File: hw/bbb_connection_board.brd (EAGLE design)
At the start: 100 x 80 mm, 2 parts, among them P8 MA23-2

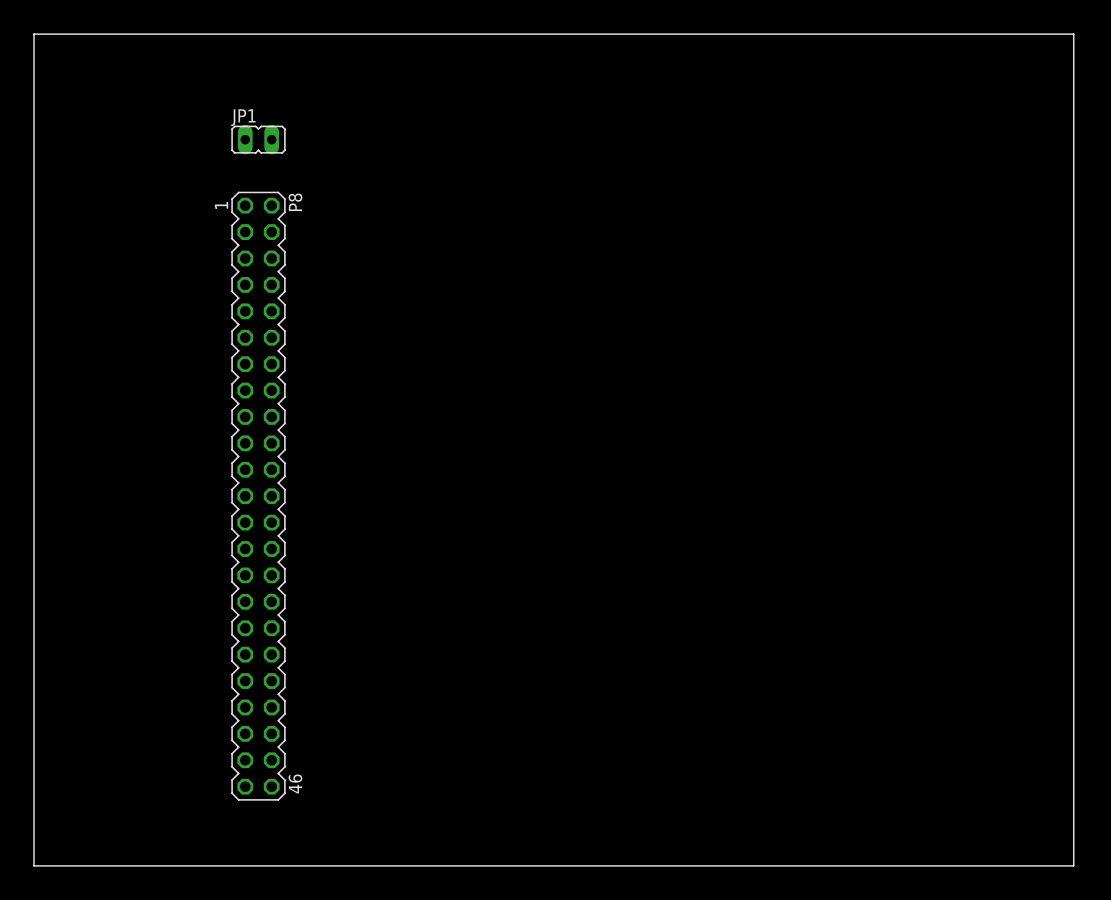
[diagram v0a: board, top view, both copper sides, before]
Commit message: schematic of bbb connection board
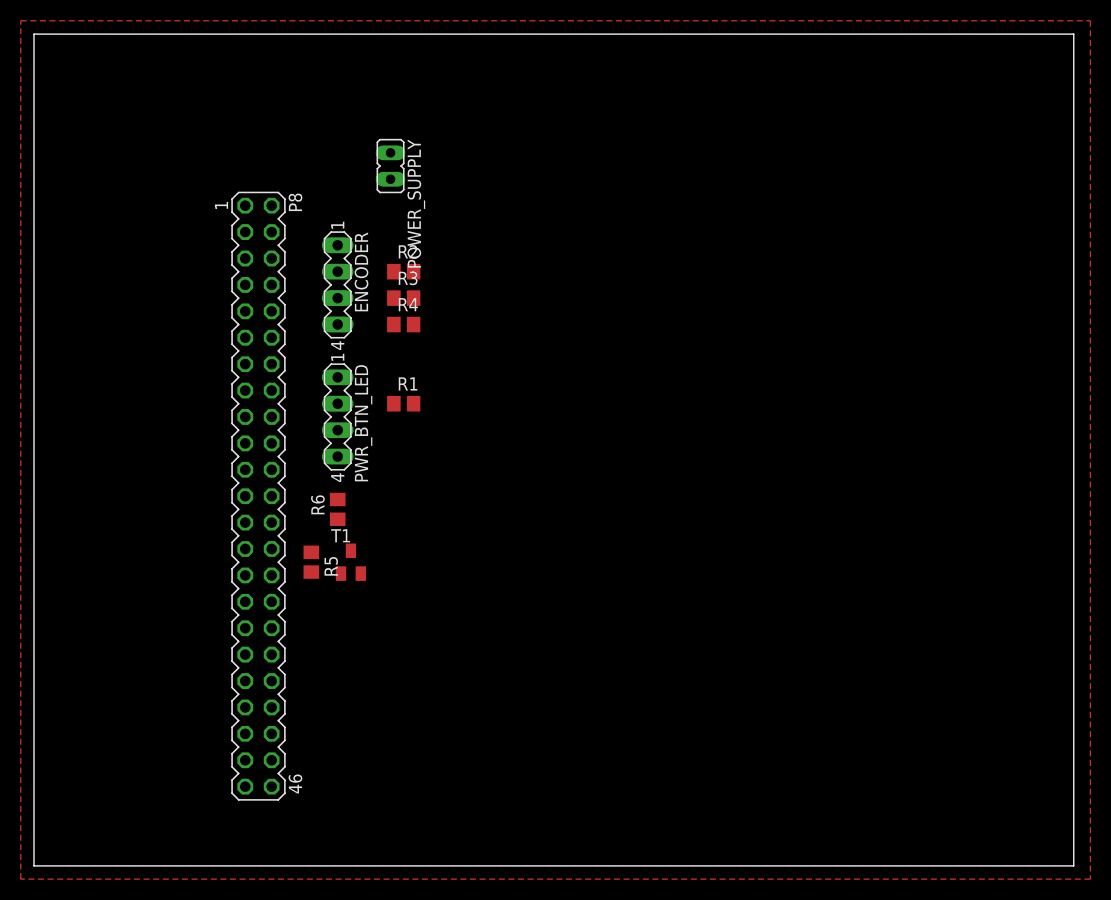
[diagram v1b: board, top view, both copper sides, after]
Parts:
- removed JP1: (no value), jumper:JP1
- added ENCODER, PWR_BTN_LED: (no value), con-lstb:MA04-1
- added POWER_SUPPLY: (no value), jumper:JP1
- added R1, R2, R3, R4, R5: 10k, rcl:R0805
- added R6: 330R, rcl:R0805
- added T1: (no value), transistor:SOT23-BEC
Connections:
- removed net ENCODER_TASTER: P8.8
- removed net PWR_TASTER: P8.7
- new net ENCODER_BTN: ENCODER.2, P8.8, R2.1
- new net LED_OUT: PWR_BTN_LED.4, R6.2
- new net N$1: R5.2, T1.B
- new net N$3: R6.1, T1.C
- new net PWR_BTN: P8.7, PWR_BTN_LED.2, R1.1
- net +3V3: now also POWER_SUPPLY.2, PWR_BTN_LED.3, R1.2, R2.2, R3.2, R4.2; no longer JP1.2
- net ENCODER_A: now also ENCODER.3, R3.1
- net ENCODER_B: now also ENCODER.4, R4.1
- net GND: now also ENCODER.1, POWER_SUPPLY.1, PWR_BTN_LED.1, T1.E; no longer JP1.1
- net PWR_LED: now also R5.1
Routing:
- added copper zone on layer 1, net GND
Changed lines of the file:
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@@
 <setting verticaltext="up"/>
 </settings>
-<grid distance="0.05" unitdist="inch" unit="inch" style="lines" multiple="1" display="yes" altdistance="0.025" altunitdist="inch" altunit="inch"/>
+<grid distance="0.05" unitdist="inch" unit="mil" style="lines" multiple="1" display="yes" altdistance="0.025" altunitdist="inch" altunit="inch"/>
 <layers>
 <layer number="1" name="Top" color="4" fill="1" visible="yes" active="yes"/>
@@
 <elements>
 <element name="P8" library="con-lstb-mod" package="MA23-2" value="MA23-2" x="20.32" y="63.5" rot="R270"/>
-<element name="JP1" library="jumper" package="JP1" value="" x="21.59" y="69.85" rot="R270"/>
+<element name="POWER_SUPPLY" library="jumper" package="JP1" value="" x="34.29" y="67.31" rot="R180"/>
+<element name="R1" library="rcl" package="R0805" value="10k" x="35.56" y="44.45"/>
+<element name="R2" library="rcl" package="R0805" value="10k" x="35.56" y="57.15"/>
+<element name="R3" library="rcl" package="R0805" value="10k" x="35.56" y="54.61"/>
+<element name="R4" library="rcl" package="R0805" value="10k" x="35.56" y="52.07"/>
+<element name="ENCODER" library="con-lstb" package="MA04-1" value="" x="29.21" y="55.88" rot="R270">
+<attribute name="OC_NEWARK" value="unknown" x="29.21" y="55.88" size="1.778" layer="27" rot="R270" display="off"/>
+<attribute name="MPN" value="" x="29.21" y="55.88" size="1.778" layer="27" rot="R270" display="off"/>
+<attribute name="MF" value="" x="29.21" y="55.88" size="1.778" layer="27" rot="R270" display="off"/>
+<attribute name="OC_FARNELL" value="unknown" x="29.21" y="55.88" size="1.778" layer="27" rot="R270" display="off"/>
+</element>
+<element name="PWR_BTN_LED" library="con-lstb" package="MA04-1" value="" x="29.21" y="43.18" rot="R270">
+<attribute name="OC_NEWARK" value="unknown" x="29.21" y="43.18" size="1.778" layer="27" rot="R270" display="off"/>
+<attribute name="MPN" value="" x="29.21" y="43.18" size="1.778" layer="27" rot="R270" display="off"/>
+<attribute name="MF" value="" x="29.21" y="43.18" size="1.778" layer="27" rot="R270" display="off"/>
+<attribute name="OC_FARNELL" value="unknown" x="29.21" y="43.18" size="1.778" layer="27" rot="R270" display="off"/>
+</element>
+<element name="T1" library="transistor" package="SOT23-BEC" value="" x="30.48" y="29.21"/>
+<element name="R5" library="rcl" package="R0805" value="10k" x="26.67" y="29.21" rot="R270"/>
+<element name="R6" library="rcl" package="R0805" value="330R" x="29.21" y="34.29" rot="R90"/>
 </elements>
 <signals>
@@
 <contactref element="P8" pad="1"/>
 <contactref element="P8" pad="2"/>
-<contactref element="JP1" pad="1"/>
-<wire x1="20.32" y1="63.5" x2="22.86" y2="63.5" width="0" layer="19" extent="1-1"/>
-<wire x1="20.32" y1="69.85" x2="22.86" y2="63.5" width="0" layer="19" extent="1-1"/>
+<contactref element="POWER_SUPPLY" pad="1"/>
+<polygon width="0.3048" layer="1">
+<vertex x="-1.27" y="81.28"/>
+<vertex x="101.6" y="81.28"/>
+<vertex x="101.6" y="-1.27"/>
+<vertex x="-1.27" y="-1.27"/>
+</polygon>
+<contactref element="ENCODER" pad="1"/>
+<contactref element="PWR_BTN_LED" pad="1"/>
+<contactref element="T1" pad="E"/>
 </signal>
 <signal name="+3V3">
-<contactref element="JP1" pad="2"/>
+<contactref element="POWER_SUPPLY" pad="2"/>
+<contactref element="R1" pad="2"/>
+<contactref element="R2" pad="2"/>
+<contactref element="R3" pad="2"/>
+<contactref element="R4" pad="2"/>
+<contactref element="PWR_BTN_LED" pad="3"/>
+<wire x1="36.51" y1="57.15" x2="34.29" y2="66.04" width="0" layer="19" extent="1-1"/>
+<wire x1="36.51" y1="54.61" x2="36.51" y2="57.15" width="0" layer="19" extent="1-1"/>
+<wire x1="36.51" y1="52.07" x2="36.51" y2="54.61" width="0" layer="19" extent="1-1"/>
+<wire x1="36.51" y1="44.45" x2="36.51" y2="52.07" width="0" layer="19" extent="1-1"/>
+<wire x1="29.21" y1="41.91" x2="36.51" y2="44.45" width="0" layer="19" extent="1-1"/>
 </signal>
 <signal name="PWR_LED">
 <contactref element="P8" pad="19"/>
+<contactref element="R5" pad="1"/>
+<wire x1="26.67" y1="30.16" x2="20.32" y2="40.64" width="0" layer="19" extent="1-1"/>
 </signal>
 <signal name="ENCODER_B">
 <contactref element="P8" pad="11"/>
+<contactref element="R4" pad="1"/>
+<contactref element="ENCODER" pad="4"/>
+<wire x1="29.21" y1="52.07" x2="34.61" y2="52.07" width="0" layer="19" extent="1-1"/>
+<wire x1="20.32" y1="50.8" x2="29.21" y2="52.07" width="0" layer="19" extent="1-1"/>
 </signal>
 <signal name="ENCODER_A">
 <contactref element="P8" pad="12"/>
-</signal>
-<signal name="PWR_TASTER">
+<contactref element="R3" pad="1"/>
+<contactref element="ENCODER" pad="3"/>
+<wire x1="29.21" y1="54.61" x2="34.61" y2="54.61" width="0" layer="19" extent="1-1"/>
+<wire x1="22.86" y1="50.8" x2="29.21" y2="54.61" width="0" layer="19" extent="1-1"/>
+</signal>
+<signal name="PWR_BTN">
 <contactref element="P8" pad="7"/>
-</signal>
-<signal name="ENCODER_TASTER">
+<contactref element="R1" pad="1"/>
+<contactref element="PWR_BTN_LED" pad="2"/>
+<wire x1="29.21" y1="44.45" x2="20.32" y2="55.88" width="0" layer="19" extent="1-1"/>
+<wire x1="34.61" y1="44.45" x2="29.21" y2="44.45" width="0" layer="19" extent="1-1"/>
+</signal>
+<signal name="ENCODER_BTN">
 <contactref element="P8" pad="8"/>
+<contactref element="R2" pad="1"/>
+<contactref element="ENCODER" pad="2"/>
+<wire x1="29.21" y1="57.15" x2="34.61" y2="57.15" width="0" layer="19" extent="1-1"/>
+<wire x1="22.86" y1="55.88" x2="29.21" y2="57.15" width="0" layer="19" extent="1-1"/>
+</signal>
+<signal name="N$1">
+<contactref element="T1" pad="B"/>
+<contactref element="R5" pad="2"/>
+<wire x1="26.67" y1="28.26" x2="29.53" y2="28.11" width="0" layer="19" extent="1-1"/>
+</signal>
+<signal name="N$3">
+<contactref element="T1" pad="C"/>
+<contactref element="R6" pad="1"/>
+<wire x1="30.48" y1="30.31" x2="29.21" y2="33.34" width="0" layer="19" extent="1-1"/>
+</signal>
+<signal name="LED_OUT">
+<contactref element="R6" pad="2"/>
+<contactref element="PWR_BTN_LED" pad="4"/>
+<wire x1="29.21" y1="35.24" x2="29.21" y2="39.37" width="0" layer="19" extent="1-1"/>
 </signal>
 </signals>

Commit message: bbb connection board routed
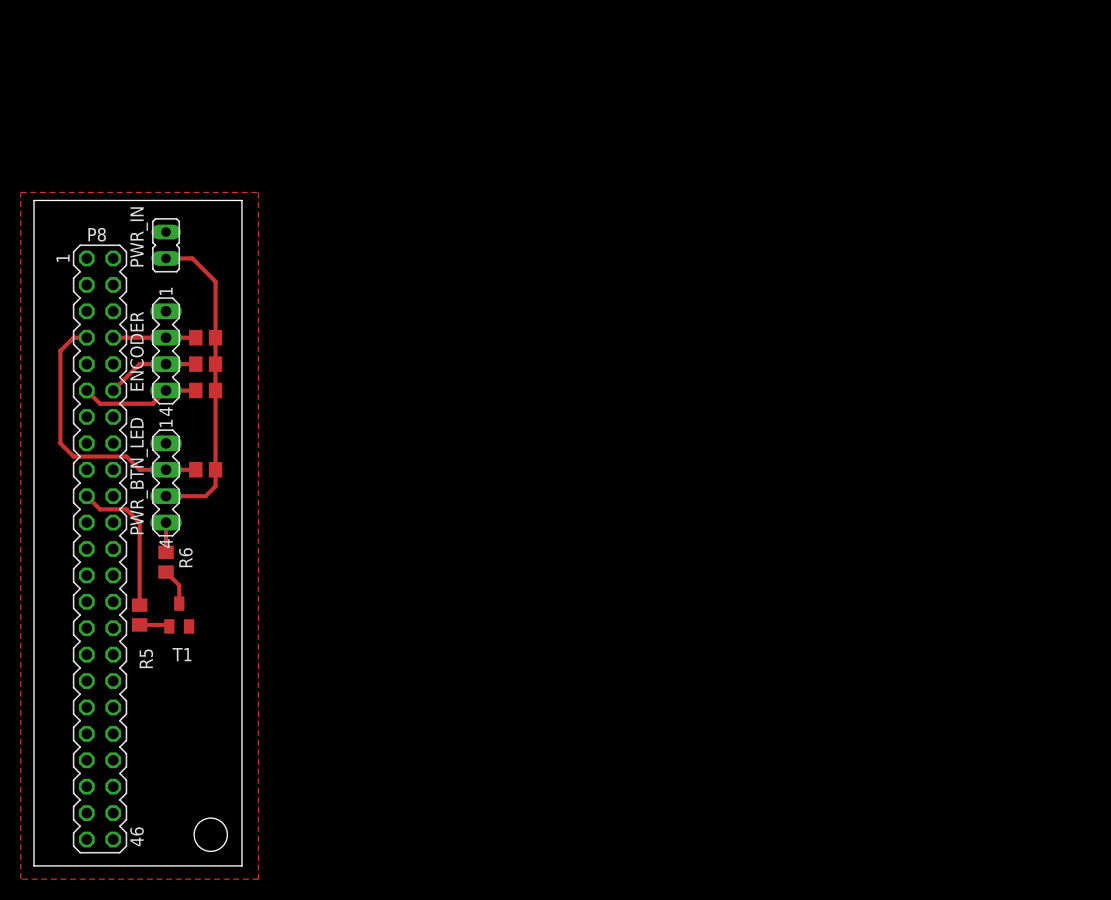
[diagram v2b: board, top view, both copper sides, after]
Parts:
- removed POWER_SUPPLY: (no value), jumper:JP1
- added PWR_IN: (no value), jumper:JP1
- moved R1 20.1 mm to (16.5, 38.1)
- moved R2 20.1 mm to (16.5, 50.8)
- moved R3 20.1 mm to (16.5, 48.3)
- moved R4 20.1 mm to (16.5, 45.7)
- moved ENCODER 17.7 mm to (12.7, 49.5)
- moved PWR_BTN_LED 17.7 mm to (12.7, 36.8)
- moved R5 17.3 mm to (10.2, 24.1)
- moved R6 17.3 mm to (12.7, 29.2)
- moved T1 17.3 mm to (14.0, 24.1)
- moved P8 16.1 mm to (5.08, 58.4)
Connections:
- net +3V3: now also PWR_IN.2; no longer POWER_SUPPLY.2
- net GND: now also PWR_IN.1; no longer POWER_SUPPLY.1
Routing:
- net +3V3: track 0.00 -> 30.5 mm
- net PWR_BTN: track 0.00 -> 26.0 mm
- net PWR_LED: track 0.00 -> 14.1 mm
- net ENCODER_B: track 0.00 -> 11.5 mm
- net ENCODER_A: track 0.00 -> 8.99 mm
- net ENCODER_BTN: track 0.00 -> 7.94 mm
- net N$3: track 0.00 -> 3.56 mm
- net N$1: track 0.00 -> 2.92 mm
- net LED_OUT: track 0.00 -> 2.86 mm
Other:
- board size 100 x 80 mm -> 20 x 64 mm
